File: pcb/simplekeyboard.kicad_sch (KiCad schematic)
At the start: 4 parts, among them J1 USB_C_Receptacle_USB2.0_16P, U1 STM32F072CBT6, U2 USBLC6-2SC6

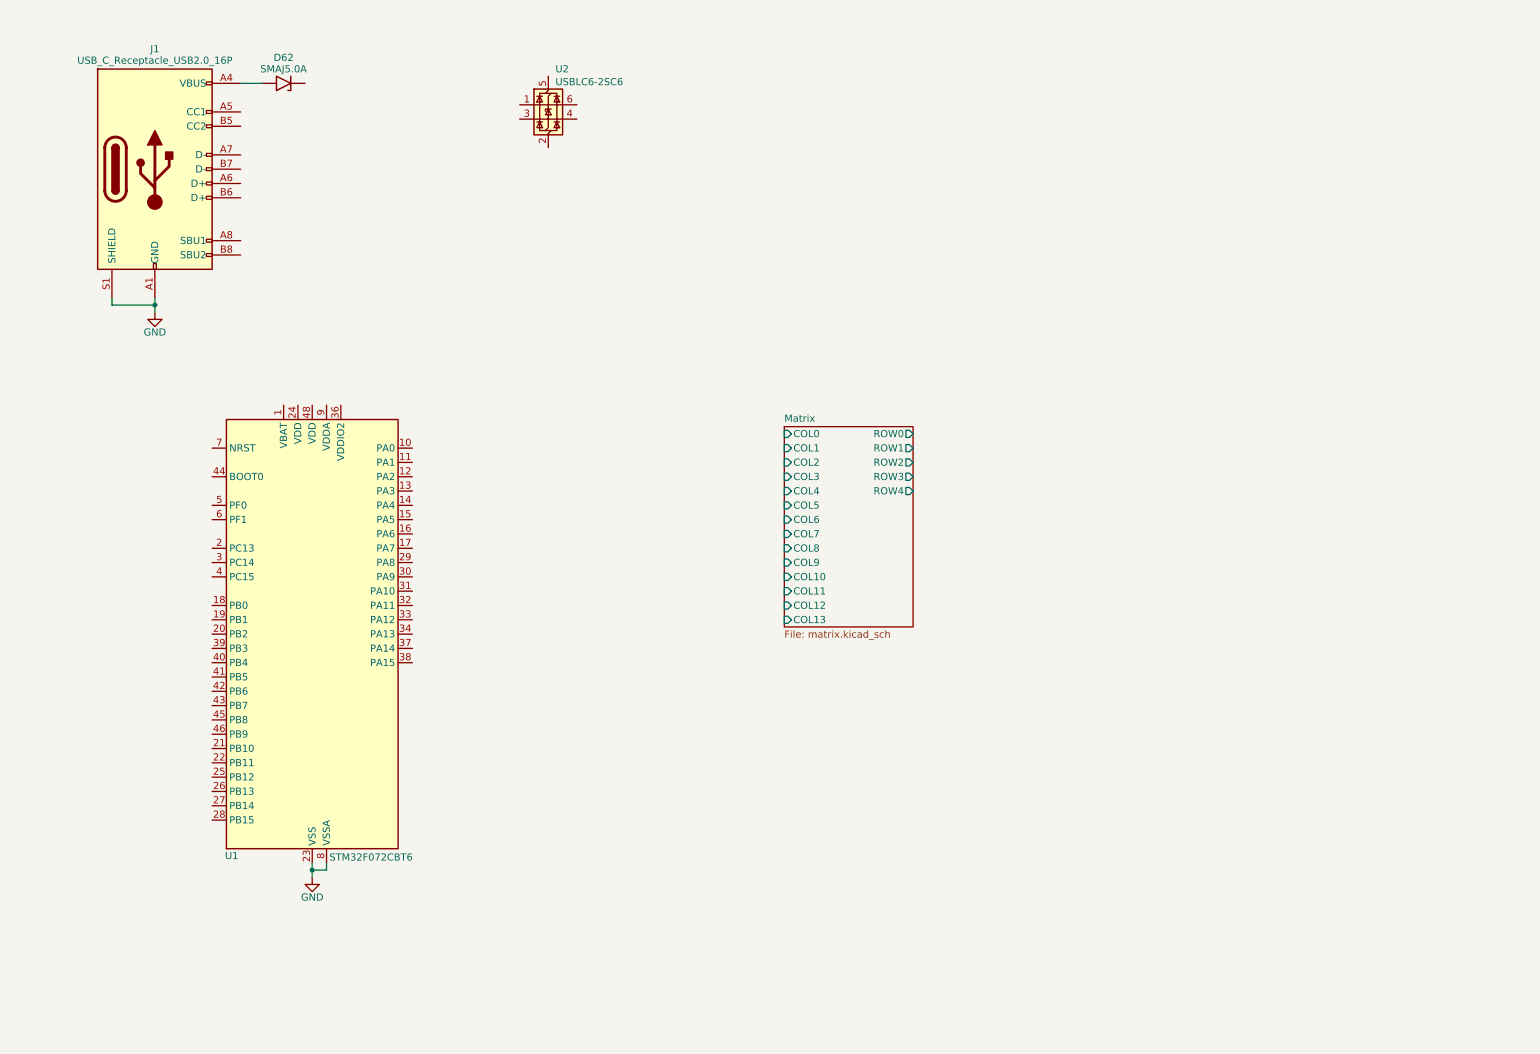
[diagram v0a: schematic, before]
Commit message: Complete MCU USB and power
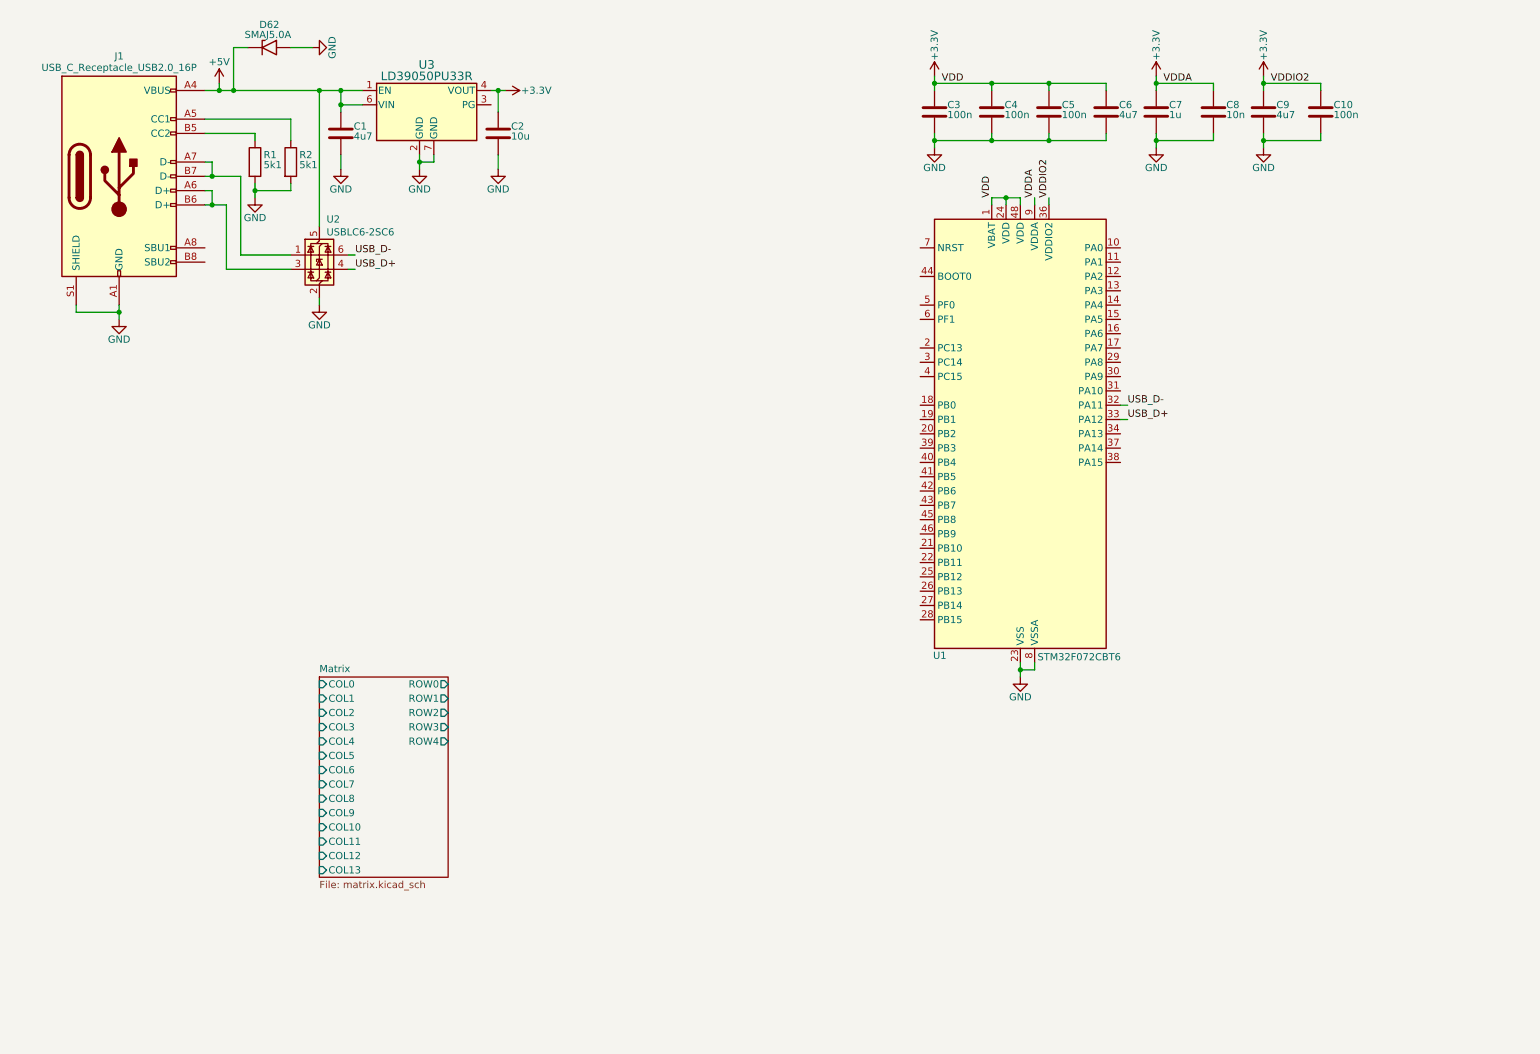
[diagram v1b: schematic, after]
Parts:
- added C1, C6, C9: 4u7, symbol Device:C
- added C10, C3, C4, C5: 100n, symbol Device:C
- added C2: 10u, symbol Device:C
- added C7: 1u, symbol Device:C
- added C8: 10n, symbol Device:C
- added R1, R2: 5k1, symbol Device:R
- added U3: LD39050PU33R, DFN6_3X3_STM, symbol Keyboard_Power:LD39050PU33R
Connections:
- net GND: now also D62.2 (A2), U2.2 (GND), C1.2, C10.2, C2.2, C3.2, C4.2, C5.2, C6.2, C7.2, C8.2, C9.2, R1.2, R2.2, U3.2 (GND), U3.7 (GND)
- net +3.3V: now reaches U1.1 (VBAT)
- net +3.3V: now also U1.24 (VDD), U1.36 (VDDIO2), U1.48 (VDD), U1.9 (VDDA), C10.1, C2.1, C3.1, C4.1, C5.1, C6.1, C7.1, C8.1, C9.1, U3.4 (VOUT)
- net USB_D-: now reaches U1.32 (PA11)
- net USB_D-: now also U2.6 (I/O1)
- net USB_D+: now reaches U1.33 (PA12)
- net USB_D+: now also U2.4 (I/O2)
- net +5V: now reaches D62.1 (A1)
- net +5V: now also J1.A4 (VBUS), J1.A9 (VBUS), J1.B4 (VBUS), J1.B9 (VBUS), U2.5 (VBUS), C1.1, U3.1 (EN), U3.6 (VIN)
- net at U2.1 (I/O1): now also J1.A7 (D-), J1.B7 (D-)
- net at U2.3 (I/O2): now also J1.A6 (D+), J1.B6 (D+)
- net at J1.A5 (CC1): now also R2.1
- net at J1.B5 (CC2): now also R1.1
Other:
- moved on the sheet: D62, J1, U1, U2

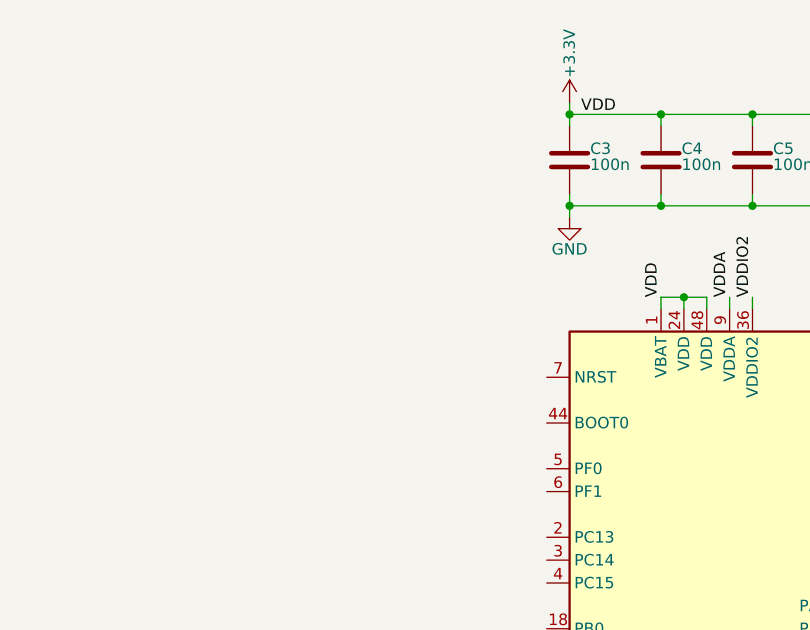
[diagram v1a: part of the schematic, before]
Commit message: Add reset and boot
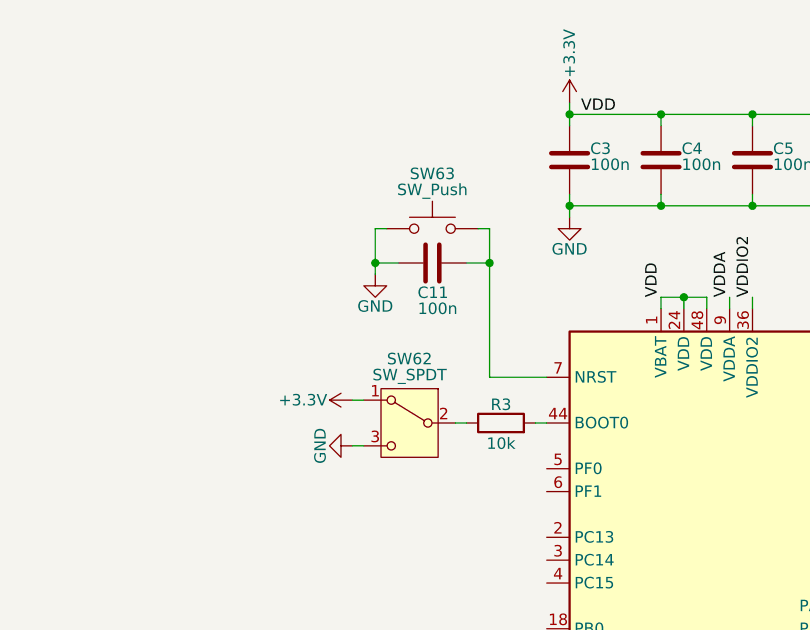
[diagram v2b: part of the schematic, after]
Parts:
- added C11: 100n, symbol Device:C
- added R3: 10k, symbol Device:R
- added SW62: SW_SPDT, symbol Switch:SW_SPDT
- added SW63: SW_Push, symbol Switch:SW_Push
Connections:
- net +3.3V: now also SW62.1 (A)
- net GND: now also C11.1, SW62.3 (C), SW63.1
- net at U1.44 (BOOT0): now also R3.2
- net at U1.7 (NRST): now also C11.2, SW63.2
- new net: R3.1, SW62.2 (B)

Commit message: Finish board schematic
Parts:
- added TP1, TP2: TestPoint, TestPoint:TestPoint_Pad_1.0x1.0mm, symbol Connector:TestPoint
- C1, C10, C11, C2, C3, C4, C5, C6, C7, C8, C9: footprint (none) -> Capacitor_SMD:C_0805_2012Metric_Pad1.18x1.45mm_HandSolder
- J1: footprint (none) -> Connector_USB:USB_C_Receptacle_HRO_TYPE-C-31-M-12
- R1, R2, R3: footprint (none) -> Resistor_SMD:R_0805_2012Metric_Pad1.20x1.40mm_HandSolder
- SW62: footprint (none) -> Button_Switch_THT:SW_Slide_SPDT_Straight_CK_OS102011MS2Q
- SW63: footprint (none) -> Button_Switch_THT:SW_PUSH_6mm
- U3: footprint DFN6_3X3_STM -> Keyboard_Power:DFN6_3X3_STM
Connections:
- net Matrix/COL0: now also U1.18 (PB0)
- net Matrix/COL1: now also U1.19 (PB1)
- net Matrix/COL10: now also U1.21 (PB10)
- net Matrix/COL11: now also U1.22 (PB11)
- net Matrix/COL12: now also U1.25 (PB12)
- net Matrix/COL13: now also U1.26 (PB13)
- net Matrix/COL2: now also U1.20 (PB2)
- net Matrix/COL3: now also U1.39 (PB3)
- net Matrix/COL4: now also U1.40 (PB4)
- net Matrix/COL5: now also U1.41 (PB5)
- net Matrix/COL6: now also U1.42 (PB6)
- net Matrix/COL7: now also U1.43 (PB7)
- net Matrix/COL8: now also U1.45 (PB8)
- net Matrix/COL9: now also U1.46 (PB9)
- net ROW0: now reaches U1.10 (PA0)
- net ROW1: now reaches U1.11 (PA1)
- net ROW2: now reaches U1.12 (PA2)
- net ROW3: now reaches U1.13 (PA3)
- net ROW4: now reaches U1.14 (PA4)
- net at U1.34 (PA13): now also TP1.1
- net at U1.37 (PA14): now also TP2.1

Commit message: Start PCB layout
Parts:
- removed D62: SMAJ5.0A, Diode_SMD:D_SMB, symbol Diode:SMAJ5.0A
- added D62: D_Zener, Diode_SMD:D_SOD-123, symbol Device:D_Zener
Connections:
- net +5V: now also D62.1 (K)
- net GND: now also D62.2 (A)

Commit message: Almost done PCB
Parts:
- C1, C10, C11, C2, C3, C4, C5, C6, C7, C8, C9: footprint Capacitor_SMD:C_0805_2012Metric_Pad1.18x1.45mm_HandSolder -> Capacitor_SMD:C_0603_1608Metric
- R1, R2, R3: footprint Resistor_SMD:R_0805_2012Metric_Pad1.20x1.40mm_HandSolder -> Resistor_SMD:R_0805_2012Metric
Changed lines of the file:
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@@
 			)
 		)
-		(property "Footprint" "Capacitor_SMD:C_0805_2012Metric_Pad1.18x1.45mm_HandSolder"
+		(property "Footprint" "Capacitor_SMD:C_0603_1608Metric"
 			(at 73.3552 39.37 0)
 			(effects
@@
 			)
 		)
-		(property "Footprint" "Capacitor_SMD:C_0805_2012Metric_Pad1.18x1.45mm_HandSolder"
+		(property "Footprint" "Capacitor_SMD:C_0603_1608Metric"
 			(at 209.2452 35.56 0)
 			(effects
@@
 			)
 		)
-		(property "Footprint" "Resistor_SMD:R_0805_2012Metric_Pad1.20x1.40mm_HandSolder"
+		(property "Footprint" "Resistor_SMD:R_0805_2012Metric"
 			(at 55.372 40.64 90)
 			(effects
@@
 			)
 		)
-		(property "Footprint" "Capacitor_SMD:C_0805_2012Metric_Pad1.18x1.45mm_HandSolder"
+		(property "Footprint" "Capacitor_SMD:C_0603_1608Metric"
 			(at 166.37 42.2148 0)
 			(effects
@@
 			)
 		)
-		(property "Footprint" "Capacitor_SMD:C_0805_2012Metric_Pad1.18x1.45mm_HandSolder"
+		(property "Footprint" "Capacitor_SMD:C_0603_1608Metric"
 			(at 188.9252 35.56 0)
 			(effects
@@
 			)
 		)
-		(property "Footprint" "Capacitor_SMD:C_0805_2012Metric_Pad1.18x1.45mm_HandSolder"
+		(property "Footprint" "Capacitor_SMD:C_0603_1608Metric"
 			(at 247.3452 35.56 0)
 			(effects
@@
 			)
 		)
-		(property "Footprint" "Capacitor_SMD:C_0805_2012Metric_Pad1.18x1.45mm_HandSolder"
+		(property "Footprint" "Capacitor_SMD:C_0603_1608Metric"
 			(at 199.0852 35.56 0)
 			(effects
@@
 			)
 		)
-		(property "Footprint" "Resistor_SMD:R_0805_2012Metric_Pad1.20x1.40mm_HandSolder"
+		(property "Footprint" "Resistor_SMD:R_0805_2012Metric"
 			(at 170.18 62.738 90)
 			(effects
@@
 			)
 		)
-		(property "Footprint" "Capacitor_SMD:C_0805_2012Metric_Pad1.18x1.45mm_HandSolder"
+		(property "Footprint" "Capacitor_SMD:C_0603_1608Metric"
 			(at 237.1852 35.56 0)
 			(effects
@@
 			)
 		)
-		(property "Footprint" "Capacitor_SMD:C_0805_2012Metric_Pad1.18x1.45mm_HandSolder"
+		(property "Footprint" "Capacitor_SMD:C_0603_1608Metric"
 			(at 228.2952 35.56 0)
 			(effects
@@
 			)
 		)
-		(property "Footprint" "Resistor_SMD:R_0805_2012Metric_Pad1.20x1.40mm_HandSolder"
+		(property "Footprint" "Resistor_SMD:R_0805_2012Metric"
 			(at 61.722 40.64 90)
 			(effects
@@
 			)
 		)
-		(property "Footprint" "Capacitor_SMD:C_0805_2012Metric_Pad1.18x1.45mm_HandSolder"
+		(property "Footprint" "Capacitor_SMD:C_0603_1608Metric"
 			(at 101.2952 39.37 0)
 			(effects
@@
 			)
 		)
-		(property "Footprint" "Capacitor_SMD:C_0805_2012Metric_Pad1.18x1.45mm_HandSolder"
+		(property "Footprint" "Capacitor_SMD:C_0603_1608Metric"
 			(at 178.7652 35.56 0)
 			(effects
@@
 			)
 		)
-		(property "Footprint" "Capacitor_SMD:C_0805_2012Metric_Pad1.18x1.45mm_HandSolder"
+		(property "Footprint" "Capacitor_SMD:C_0603_1608Metric"
 			(at 218.1352 35.56 0)
 			(effects
